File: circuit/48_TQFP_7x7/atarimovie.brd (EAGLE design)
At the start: 72.4 x 82.5 mm, 24 parts, among them IC1 AMS1117-3.3V, J1 CARTRIDGE EDGE, J2 TF-15X15, U1 DSPIC33CKXXMC105-X_M4TQFP48_7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, U2 74LVCH245APW,118, U3 74LVCH245APW,118, X1 22-23-2051

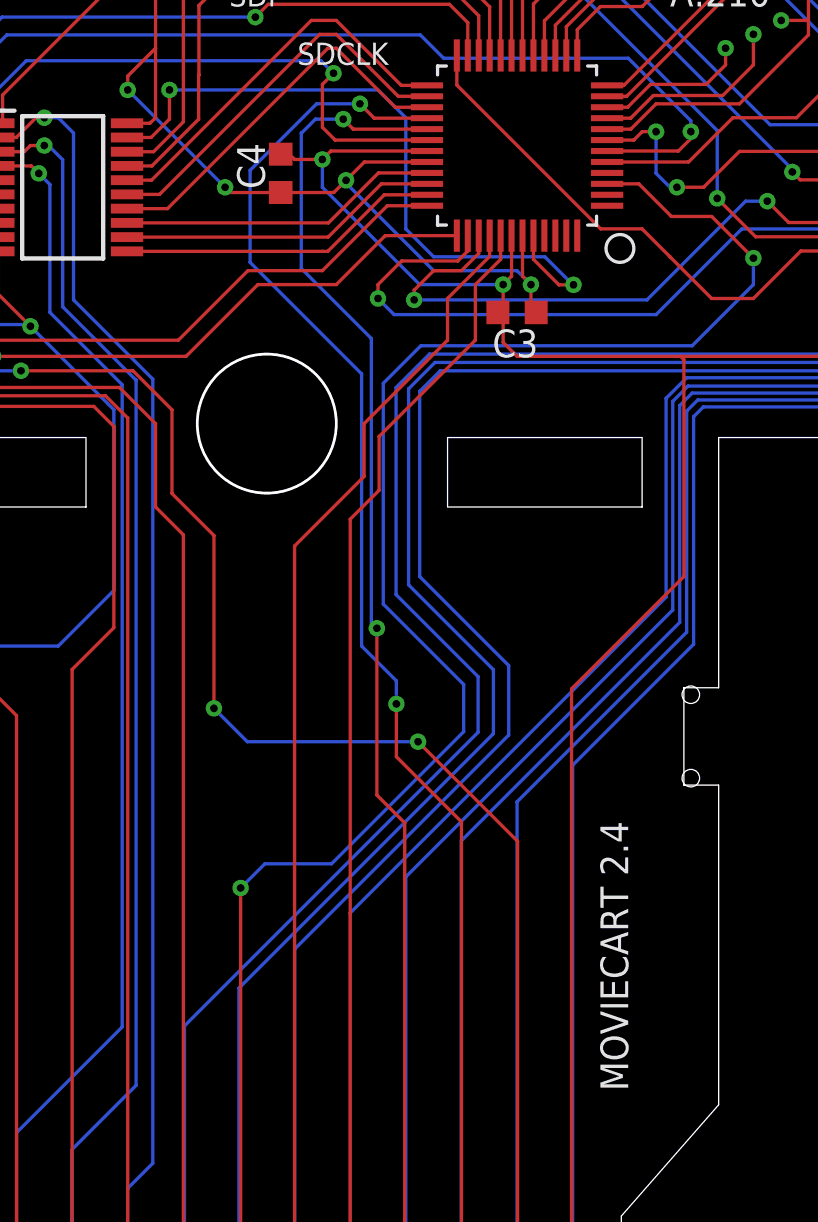
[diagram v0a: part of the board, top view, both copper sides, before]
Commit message: PCB: slightly widened post hole from 3.175 to 3.210 mm
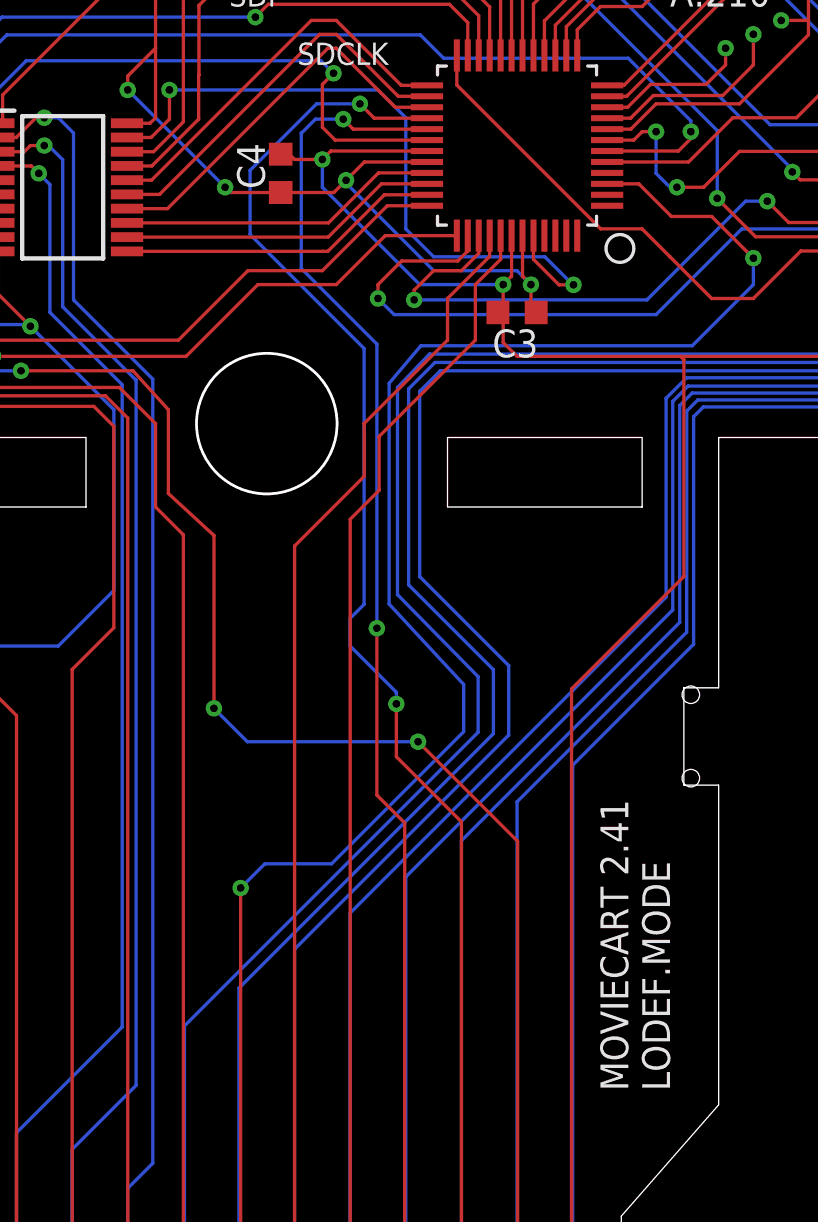
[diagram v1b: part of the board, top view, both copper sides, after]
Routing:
- net CADDR8: track 72.8 -> 73.3 mm
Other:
- board text added: "LODEF.MODE"
- board text added: "MOVIECART 2.41"
- board text removed: "MOVIECART 2.4"
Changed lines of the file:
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@@
 <board>
 <plain>
-<text x="53.34" y="20.955" size="1.27" layer="21" font="vector" rot="R90">MOVIECART 2.4</text>
+<text x="53.34" y="20.955" size="1.27" layer="21" font="vector" rot="R90">MOVIECART 2.41</text>
 <text x="14.6685" y="76.835" size="1.016" layer="21" rot="R270">VPP</text>
 <text x="12.065" y="76.835" size="1.016" layer="21" rot="R270">VDD</text>
@@
 <text x="56.0705" y="75.2475" size="1.016" layer="25">SDCS</text>
 <text x="19.1135" y="59.944" size="1.016" layer="25">SDO</text>
+<text x="55.245" y="20.955" size="1.27" layer="21" font="vector" rot="R90">LODEF.MODE</text>
 </plain>
 <attributes>
@@
 <wire x1="71.12" y1="64.73915" x2="71.12" y2="64.77" width="0.1524" layer="1"/>
 <wire x1="69.59924375" y1="63.21839375" x2="71.12" y2="64.73915" width="0.1524" layer="1"/>
-<wire x1="42.7355" y1="43.6245" x2="42.7355" y2="53.086" width="0.1524" layer="16"/>
-<wire x1="42.7355" y1="53.086" x2="44.2595" y2="54.61" width="0.1524" layer="16"/>
+<wire x1="42.799" y1="43.6245" x2="42.799" y2="53.086" width="0.1524" layer="16"/>
+<wire x1="42.799" y1="53.086" x2="44.2595" y2="54.61" width="0.1524" layer="16"/>
 <wire x1="63.5" y1="54.61" x2="44.2595" y2="54.61" width="0.1524" layer="16"/>
 <wire x1="66.929" y1="58.039" x2="63.5" y2="54.61" width="0.1524" layer="16"/>
 <wire x1="46.482" y1="37.338" x2="46.482" y2="39.878" width="0.1524" layer="16"/>
-<wire x1="46.482" y1="39.878" x2="42.7355" y2="43.6245" width="0.1524" layer="16"/>
+<wire x1="46.482" y1="39.878" x2="42.799" y2="43.6245" width="0.1524" layer="16"/>
 </signal>
 <signal name="CADDR1">
@@
 <wire x1="41.0845" y1="66.04" x2="39.1033" y2="66.04" width="0.1524" layer="16"/>
 <via x="42.7482" y="38.6334" extent="1-16" drill="0.35"/>
-<wire x1="36.068" y1="58.801" x2="36.068" y2="63.0047" width="0.1524" layer="16"/>
+<wire x1="36.068" y1="60.071" x2="36.068" y2="63.0047" width="0.1524" layer="16"/>
 <wire x1="39.1033" y1="66.04" x2="36.068" y2="63.0047" width="0.1524" layer="16"/>
-<wire x1="41.1607" y1="41.275" x2="41.1607" y2="53.7083" width="0.1524" layer="16"/>
-<wire x1="41.1607" y1="53.7083" x2="36.068" y2="58.801" width="0.1524" layer="16"/>
-<wire x1="42.7482" y1="38.6334" x2="42.7482" y2="39.6875" width="0.1524" layer="16"/>
-<wire x1="42.7482" y1="39.6875" x2="41.1607" y2="41.275" width="0.1524" layer="16"/>
+<wire x1="41.275" y1="54.864" x2="36.068" y2="60.071" width="0.1524" layer="16"/>
 <wire x1="44.1452" y1="65.385" x2="41.7395" y2="65.385" width="0.1524" layer="1"/>
 <wire x1="41.7395" y1="65.385" x2="41.0845" y2="66.04" width="0.1524" layer="1"/>
+<wire x1="41.275" y1="54.864" x2="41.275" y2="43.18" width="0.1524" layer="16"/>
+<wire x1="41.275" y1="43.18" x2="40.64" y2="42.545" width="0.1524" layer="16"/>
+<wire x1="40.64" y1="42.545" x2="40.64" y2="41.275" width="0.1524" layer="16"/>
+<wire x1="42.7482" y1="38.6334" x2="42.7482" y2="39.1668" width="0.1524" layer="16"/>
+<wire x1="42.7482" y1="39.1668" x2="40.64" y2="41.275" width="0.1524" layer="16"/>
 </signal>
 <signal name="CADDR9">
@@
 <contactref element="U1" pad="29"/>
 <via x="40.3225" y="65.3415" extent="1-16" drill="0.35"/>
-<wire x1="38.4048" y1="58.5216" x2="38.4048" y2="64.7065" width="0.1524" layer="16"/>
+<wire x1="38.4048" y1="64.7065" x2="38.4048" y2="58.5216" width="0.1524" layer="16"/>
 <wire x1="39.0525" y1="65.3415" x2="38.4175" y2="64.7065" width="0.1524" layer="16"/>
 <wire x1="39.0525" y1="65.3415" x2="40.3225" y2="65.3415" width="0.1524" layer="16"/>
@@
 <wire x1="43.18" y1="3.81" x2="43.1292" y2="3.81" width="0.1524" layer="1"/>
 <via x="41.8592" y="42.0878" extent="1-16" drill="0.35"/>
-<wire x1="41.6052" y1="55.3212" x2="41.6052" y2="42.3418" width="0.1524" layer="16"/>
-<wire x1="41.8592" y1="42.0878" x2="41.6052" y2="42.3418" width="0.1524" layer="16"/>
-<wire x1="41.6052" y1="55.3212" x2="38.4048" y2="58.5216" width="0.1524" layer="16"/>
 <wire x1="43.1292" y1="33.1978" x2="41.8592" y2="34.4678" width="0.1524" layer="1"/>
 <wire x1="41.8592" y1="34.4678" x2="41.8592" y2="42.0878" width="0.1524" layer="1"/>
@@
 <wire x1="44.1452" y1="64.885" x2="40.779" y2="64.885" width="0.1524" layer="1"/>
 <wire x1="40.779" y1="64.885" x2="40.3225" y2="65.3415" width="0.1524" layer="1"/>
+<wire x1="41.8592" y1="55.0672" x2="41.8592" y2="42.0878" width="0.1524" layer="16"/>
+<wire x1="38.4048" y1="58.5216" x2="41.8592" y2="55.0672" width="0.1524" layer="16"/>
 </signal>
 <signal name="CADDR10">
@@
 <wire x1="57.15" y1="60.8965" x2="55.3085" y2="60.8965" width="0.1524" layer="1"/>
 <wire x1="57.15" y1="60.8965" x2="59.055" y2="58.9915" width="0.1524" layer="1"/>
-<wire x1="42.1513" y1="43.1927" x2="42.1513" y2="53.2765" width="0.1524" layer="16"/>
-<wire x1="42.1513" y1="53.2765" x2="43.8658" y2="54.991" width="0.1524" layer="16"/>
+<wire x1="42.418" y1="43.1927" x2="42.418" y2="53.2765" width="0.1524" layer="16"/>
+<wire x1="42.418" y1="53.2765" x2="43.8658" y2="54.991" width="0.1524" layer="16"/>
 <wire x1="56.261" y1="54.991" x2="59.055" y2="57.785" width="0.1524" layer="16"/>
 <wire x1="43.8658" y1="54.991" x2="56.261" y2="54.991" width="0.1524" layer="16"/>
 <wire x1="39.789471875" y1="31.330528125" x2="45.821971875" y2="37.363028125" width="0.1524" layer="16"/>
 <wire x1="45.821971875" y1="37.363028125" x2="45.821971875" y2="39.522028125" width="0.1524" layer="16"/>
-<wire x1="45.821971875" y1="39.522028125" x2="42.1513" y2="43.1927" width="0.1524" layer="16"/>
+<wire x1="45.821971875" y1="39.522028125" x2="42.418" y2="43.1927" width="0.1524" layer="16"/>
 <wire x1="35.6362" y1="30.226" x2="36.740728125" y2="31.330528125" width="0.1524" layer="16"/>
 <wire x1="39.789471875" y1="31.330528125" x2="36.740728125" y2="31.330528125" width="0.1524" layer="16"/>
@@
 <via x="43.7388" y="36.9062" extent="1-16" drill="0.35"/>
 <wire x1="25.6032" y1="53.848" x2="30.7213" y2="53.848" width="0.1524" layer="1"/>
-<wire x1="30.7213" y1="53.848" x2="32.4993" y2="52.07" width="0.1524" layer="1"/>
-<wire x1="32.4993" y1="52.07" x2="32.4993" y2="48.2441625" width="0.1524" layer="1"/>
-<wire x1="32.4993" y1="48.2441625" x2="34.417" y2="46.3264625" width="0.1524" layer="1"/>
+<wire x1="30.7213" y1="53.848" x2="32.3342" y2="52.07" width="0.1524" layer="1"/>
+<wire x1="32.3342" y1="52.07" x2="32.3342" y2="48.2441625" width="0.1524" layer="1"/>
+<wire x1="32.3342" y1="48.2441625" x2="34.417" y2="46.3264625" width="0.1524" layer="1"/>
 <wire x1="34.417" y1="46.3264625" x2="34.417" y2="38.4302" width="0.1524" layer="1"/>
 <contactref element="IC1" pad="3"/>
